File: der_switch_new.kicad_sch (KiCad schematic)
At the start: 1 part, among them U1 KSZ9477S

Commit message: add TQFP-128_14x14mm_P0.4mm_EP10x10mm_ThermalVias footprint
and assign it to the ksz chip

Signed-off-by: Oleksij Rempel <linux@rempel-privat.de>
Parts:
- U1: footprint Package_QFP:TQFP-128_14x14mm_P0.4mm -> footprints:TQFP-128_14x14mm_P0.4mm_EP10x10mm_ThermalVias
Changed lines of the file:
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@@
       (effects (font (size 1.27 1.27)) (justify left))
     )
-    (property "Footprint" "Package_QFP:TQFP-128_14x14mm_P0.4mm" (id 2) (at 233.426 144.272 0)
+    (property "Footprint" "footprints:TQFP-128_14x14mm_P0.4mm_EP10x10mm_ThermalVias" (id 2) (at 233.426 144.272 0)
       (effects (font (size 1.27 1.27)) hide)
     )
@@
     (property "Reference" "U1" (id 0) (at 62.23 21.59 0))
     (property "Value" "KSZ9477S" (id 1) (at 62.23 24.13 0))
-    (property "Footprint" "Package_QFP:TQFP-128_14x14mm_P0.4mm" (id 2) (at 46.736 62.992 0)
+    (property "Footprint" "footprints:TQFP-128_14x14mm_P0.4mm_EP10x10mm_ThermalVias" (id 2) (at 46.736 62.992 0)
       (effects (font (size 1.27 1.27)) hide)
     )
@@
       (effects (font (size 1.27 1.27)) (justify left))
     )
-    (property "Footprint" "Package_QFP:TQFP-128_14x14mm_P0.4mm" (id 2) (at 182.626 126.492 0)
+    (property "Footprint" "footprints:TQFP-128_14x14mm_P0.4mm_EP10x10mm_ThermalVias" (id 2) (at 182.626 126.492 0)
       (effects (font (size 1.27 1.27)) hide)
     )
@@
   (symbol_instances
     (path "/80ef473c-1a77-4105-9e67-974a5bdd257e"
-      (reference "U1") (unit 1) (value "KSZ9477S") (footprint "Package_QFP:TQFP-128_14x14mm_P0.4mm")
+      (reference "U1") (unit 1) (value "KSZ9477S") (footprint "footprints:TQFP-128_14x14mm_P0.4mm_EP10x10mm_ThermalVias")
     )
     (path "/21ac9210-ce64-4f1c-8b3c-e40224109109"
-      (reference "U1") (unit 7) (value "KSZ9477S") (footprint "Package_QFP:TQFP-128_14x14mm_P0.4mm")
+      (reference "U1") (unit 7) (value "KSZ9477S") (footprint "footprints:TQFP-128_14x14mm_P0.4mm_EP10x10mm_ThermalVias")
     )
     (path "/8afa4008-8209-42cc-9fef-0c59ffa66b4d"
-      (reference "U1") (unit 8) (value "KSZ9477S") (footprint "Package_QFP:TQFP-128_14x14mm_P0.4mm")
+      (reference "U1") (unit 8) (value "KSZ9477S") (footprint "footprints:TQFP-128_14x14mm_P0.4mm_EP10x10mm_ThermalVias")
     )
     (path "/71aecc81-5a5e-4293-ac09-31c20a082000/64182846-cada-49dd-8527-6959da40f69f"
@@
     )
     (path "/71aecc81-5a5e-4293-ac09-31c20a082000/9e4a7f6b-5383-44a7-b0de-9b68ac0e96b4"
-      (reference "U1") (unit 9) (value "KSZ9477S") (footprint "Package_QFP:TQFP-128_14x14mm_P0.4mm")
+      (reference "U1") (unit 9) (value "KSZ9477S") (footprint "footprints:TQFP-128_14x14mm_P0.4mm_EP10x10mm_ThermalVias")
     )
     (path "/33923bc8-5675-46d6-90be-4bb312e65519/a0f59906-4c59-4b83-9dc6-53f2550f4015"
@@
     )
     (path "/33923bc8-5675-46d6-90be-4bb312e65519/3e63a1df-1271-48f3-b68c-81f417692ad7"
-      (reference "U1") (unit 6) (value "KSZ9477S") (footprint "Package_QFP:TQFP-128_14x14mm_P0.4mm")
+      (reference "U1") (unit 6) (value "KSZ9477S") (footprint "footprints:TQFP-128_14x14mm_P0.4mm_EP10x10mm_ThermalVias")
     )
     (path "/33923bc8-5675-46d6-90be-4bb312e65519/5b33dfef-7c88-4a53-adf9-8d0c01072e7c/708f89c6-cb28-4190-913e-6f6103f78790"
@@
     )
     (path "/33923bc8-5675-46d6-90be-4bb312e65519/5b33dfef-7c88-4a53-adf9-8d0c01072e7c/ff5fbc13-5ce9-4122-a56a-496076beffc2"
-      (reference "U1") (unit 2) (value "KSZ9477S") (footprint "Package_QFP:TQFP-128_14x14mm_P0.4mm")
+      (reference "U1") (unit 2) (value "KSZ9477S") (footprint "footprints:TQFP-128_14x14mm_P0.4mm_EP10x10mm_ThermalVias")
     )
     (path "/33923bc8-5675-46d6-90be-4bb312e65519/5b33dfef-7c88-4a53-adf9-8d0c01072e7c/860177f5-e5f9-4667-bdf1-260227f40112"
-      (reference "U1") (unit 3) (value "KSZ9477S") (footprint "Package_QFP:TQFP-128_14x14mm_P0.4mm")
+      (reference "U1") (unit 3) (value "KSZ9477S") (footprint "footprints:TQFP-128_14x14mm_P0.4mm_EP10x10mm_ThermalVias")
     )
     (path "/33923bc8-5675-46d6-90be-4bb312e65519/c8a14ab9-546c-463a-ad16-fe3e65a560b9/eb7b83be-b0ce-45b6-906a-1b3b0cc9f6ff"
@@
     )
     (path "/33923bc8-5675-46d6-90be-4bb312e65519/c8a14ab9-546c-463a-ad16-fe3e65a560b9/639c0f21-cd49-4621-910a-9ec66a1169ab"
-      (reference "U1") (unit 4) (value "KSZ9477S") (footprint "Package_QFP:TQFP-128_14x14mm_P0.4mm")
+      (reference "U1") (unit 4) (value "KSZ9477S") (footprint "footprints:TQFP-128_14x14mm_P0.4mm_EP10x10mm_ThermalVias")
     )
     (path "/33923bc8-5675-46d6-90be-4bb312e65519/c8a14ab9-546c-463a-ad16-fe3e65a560b9/08269ac5-7f42-4ff7-a5e8-908b55ba521c"
-      (reference "U1") (unit 5) (value "KSZ9477S") (footprint "Package_QFP:TQFP-128_14x14mm_P0.4mm")
-    )
-  )
+      (reference "U1") (unit 5) (value "KSZ9477S") (footprint "footprints:TQFP-128_14x14mm_P0.4mm_EP10x10mm_ThermalVias")
+    )
+  )

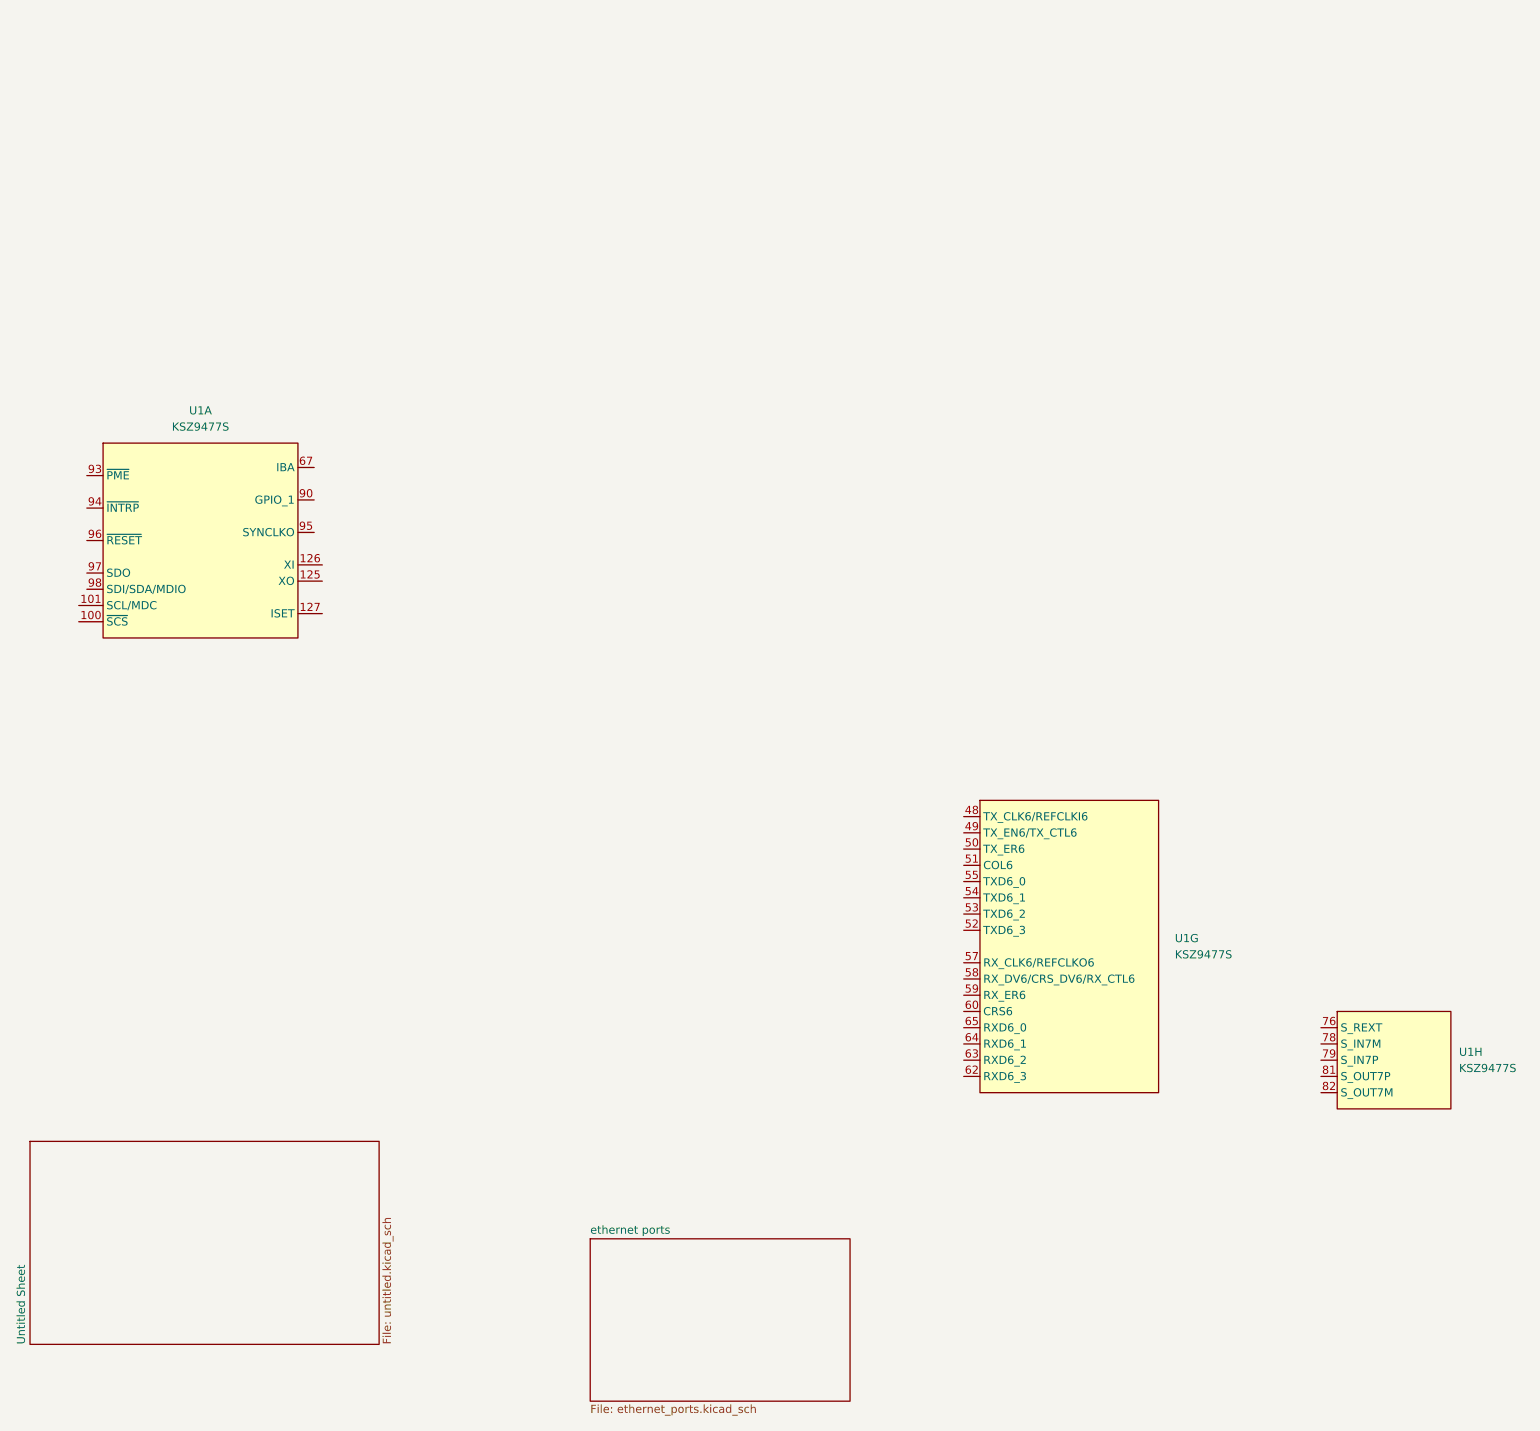
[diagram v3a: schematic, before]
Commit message: update pin naming. use _P/_N to allow optiomisation for differential signal
Signed-off-by: Oleksij Rempel <linux@rempel-privat.de>
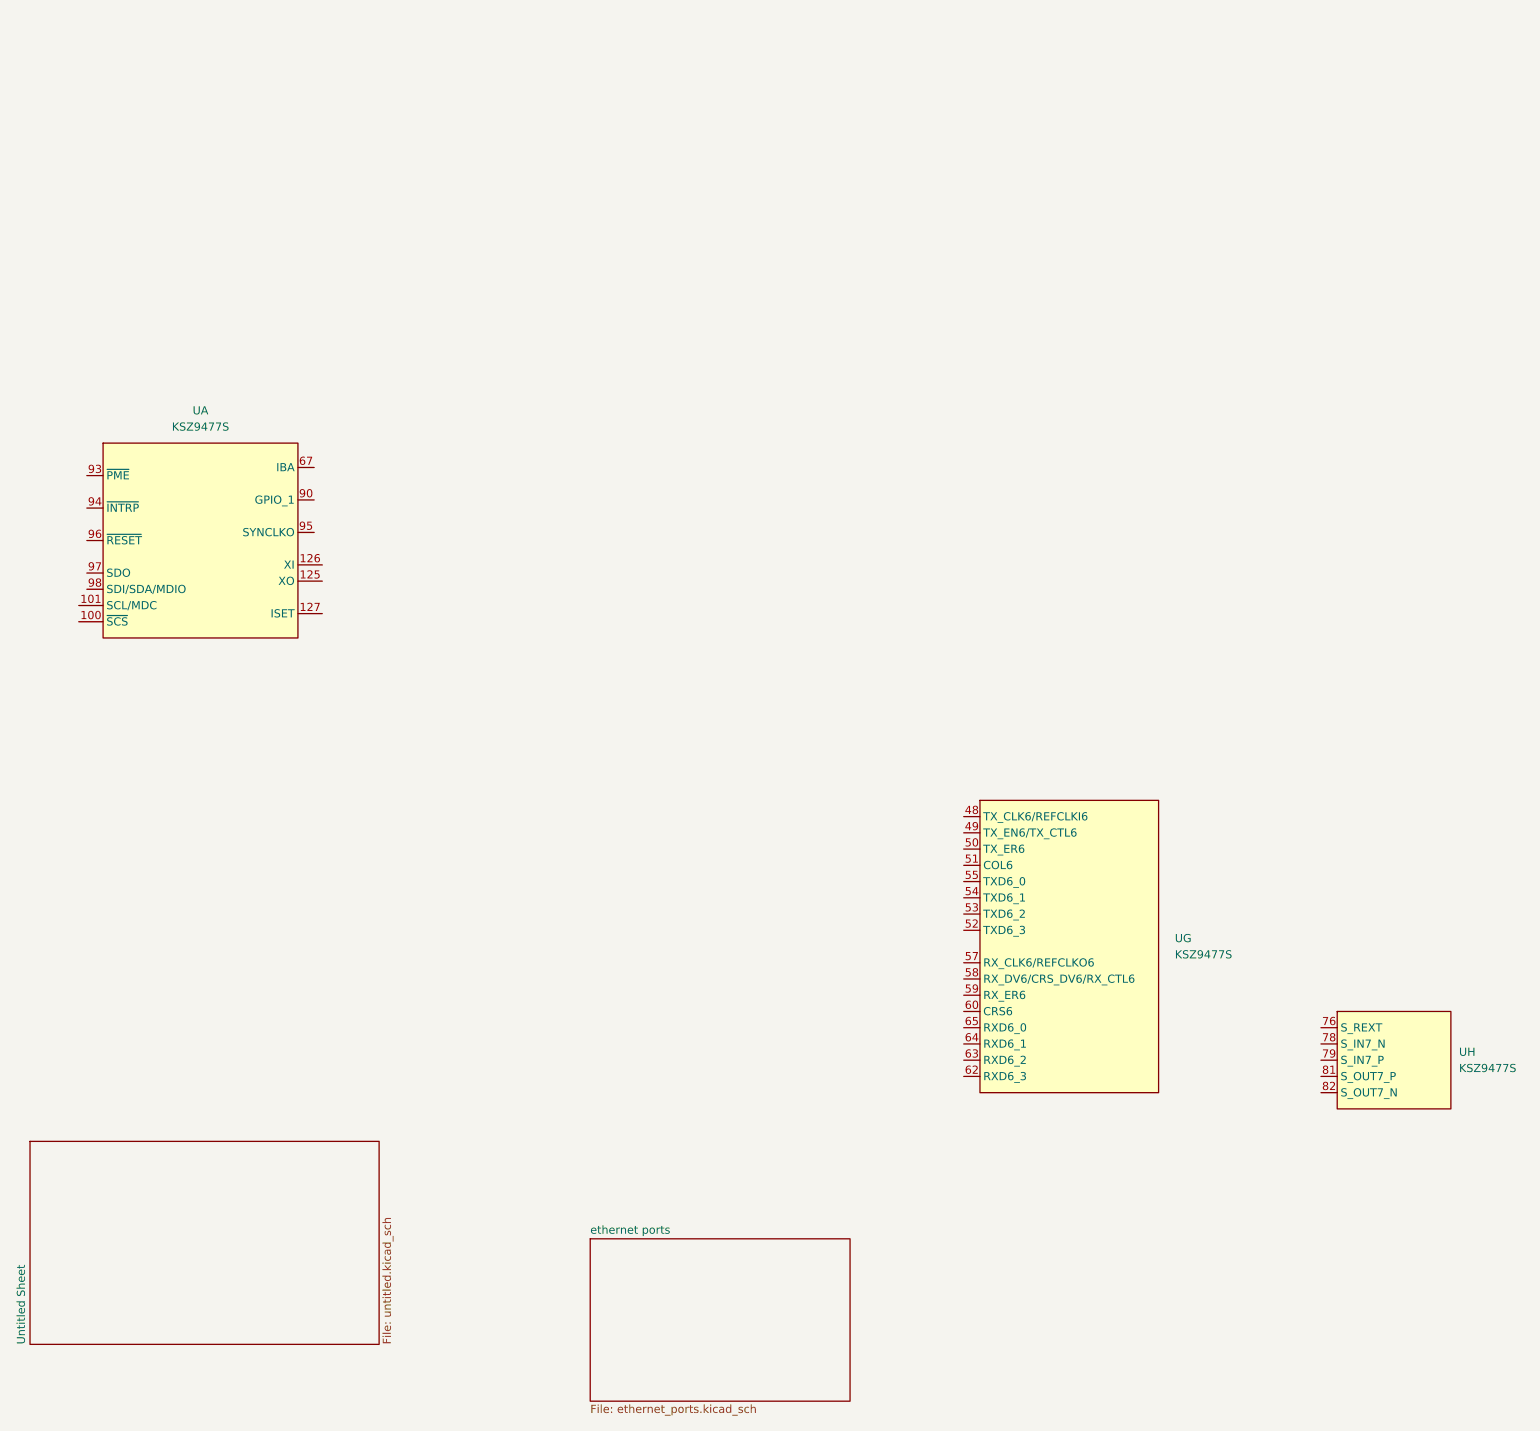
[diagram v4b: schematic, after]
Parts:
- U: renamed from U1; footprint footprints:TQFP-128_14x14mm_P0.4mm_EP10x10mm_ThermalVias -> Package_QFP:TQFP-128_14x14mm_P0.4mm
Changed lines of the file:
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@@
-(kicad_sch (version 20201015) (generator eeschema)
+(kicad_sch (version 20210126) (generator eeschema)
   (paper "A4")
-  (symbol (lib_id "local:KSZ9477S") (at 248.92 123.19 0) (unit 8)
+  (symbol (lib_name "local:KSZ9477S_2") (lib_id "local:KSZ9477S") (at 248.92 123.19 0) (unit 8)
     (in_bom yes) (on_board yes)
-    (property "Reference" "U1" (id 0) (at 259.08 121.92 0)
+    (property "Reference" "U" (id 0) (at 259.08 121.92 0)
       (effects (font (size 1.27 1.27)) (justify left))
     )
@@
       (effects (font (size 1.27 1.27)) (justify left))
     )
-    (property "Footprint" "footprints:TQFP-128_14x14mm_P0.4mm_EP10x10mm_ThermalVias" (id 2) (at 233.426 144.272 0)
+    (property "Footprint" "Package_QFP:TQFP-128_14x14mm_P0.4mm" (id 2) (at 233.426 144.272 0)
       (effects (font (size 1.27 1.27)) hide)
     )
@@
       (effects (font (size 1.27 1.27)) hide)
     )
-  )
-  (symbol (lib_id "local:KSZ9477S") (at 62.23 41.91 0) (unit 1)
+    (pin "76")
+    (pin "82")
+    (pin "81")
+    (pin "78")
+    (pin "79")
+  )
+  (symbol (lib_name "local:KSZ9477S_1") (lib_id "local:KSZ9477S") (at 62.23 41.91 0) (unit 1)
     (in_bom yes) (on_board yes)
-    (property "Reference" "U1" (id 0) (at 62.23 21.59 0))
+    (property "Reference" "U" (id 0) (at 62.23 21.59 0))
     (property "Value" "KSZ9477S" (id 1) (at 62.23 24.13 0))
-    (property "Footprint" "footprints:TQFP-128_14x14mm_P0.4mm_EP10x10mm_ThermalVias" (id 2) (at 46.736 62.992 0)
+    (property "Footprint" "Package_QFP:TQFP-128_14x14mm_P0.4mm" (id 2) (at 46.736 62.992 0)
       (effects (font (size 1.27 1.27)) hide)
     )
@@
       (effects (font (size 1.27 1.27)) hide)
     )
+    (pin "97")
+    (pin "98")
+    (pin "100")
+    (pin "101")
+    (pin "125")
+    (pin "126")
+    (pin "93")
+    (pin "94")
+    (pin "96")
+    (pin "95")
+    (pin "90")
+    (pin "127")
+    (pin "67")
+    (pin "73")
+    (pin "74")
+    (pin "108")
   )
   (symbol (lib_id "local:KSZ9477S") (at 198.12 105.41 0) (unit 7)
     (in_bom yes) (on_board yes)
-    (property "Reference" "U1" (id 0) (at 214.63 104.14 0)
+    (property "Reference" "U" (id 0) (at 214.63 104.14 0)
       (effects (font (size 1.27 1.27)) (justify left))
     )
@@
       (effects (font (size 1.27 1.27)) (justify left))
     )
-    (property "Footprint" "footprints:TQFP-128_14x14mm_P0.4mm_EP10x10mm_ThermalVias" (id 2) (at 182.626 126.492 0)
+    (property "Footprint" "Package_QFP:TQFP-128_14x14mm_P0.4mm" (id 2) (at 182.626 126.492 0)
       (effects (font (size 1.27 1.27)) hide)
     )
@@
       (effects (font (size 1.27 1.27)) hide)
     )
+    (pin "62")
+    (pin "63")
+    (pin "64")
+    (pin "65")
+    (pin "57")
+    (pin "58")
+    (pin "59")
+    (pin "52")
+    (pin "53")
+    (pin "54")
+    (pin "55")
+    (pin "48")
+    (pin "49")
+    (pin "50")
+    (pin "51")
+    (pin "60")
   )
   (sheet (at 35.56 135.89) (size 54.61 31.75)
@@
       (effects (font (size 1.27 1.27)) (justify left bottom))
     )
-    (property "Sheet file" "untitled.kicad_sch" (id 1) (at 90.6789 167.64 90)
+    (property "Dateiname Blatt" "untitled.kicad_sch" (id 1) (at 90.6789 167.64 90)
       (effects (font (size 1.27 1.27)) (justify left top))
     )
@@
       (effects (font (size 1.27 1.27)) (justify left bottom))
     )
-    (property "Sheet file" "ethernet_ports.kicad_sch" (id 1) (at 123.19 177.0389 0)
+    (property "Dateiname Blatt" "ethernet_ports.kicad_sch" (id 1) (at 123.19 177.0389 0)
       (effects (font (size 1.27 1.27)) (justify left top))
     )
@@
   (symbol_instances
     (path "/80ef473c-1a77-4105-9e67-974a5bdd257e"
-      (reference "U1") (unit 1) (value "KSZ9477S") (footprint "footprints:TQFP-128_14x14mm_P0.4mm_EP10x10mm_ThermalVias")
+      (reference "U") (unit 1) (value "KSZ9477S") (footprint "Package_QFP:TQFP-128_14x14mm_P0.4mm")
     )
     (path "/21ac9210-ce64-4f1c-8b3c-e40224109109"
-      (reference "U1") (unit 7) (value "KSZ9477S") (footprint "footprints:TQFP-128_14x14mm_P0.4mm_EP10x10mm_ThermalVias")
+      (reference "U") (unit 7) (value "KSZ9477S") (footprint "Package_QFP:TQFP-128_14x14mm_P0.4mm")
     )
     (path "/8afa4008-8209-42cc-9fef-0c59ffa66b4d"
-      (reference "U1") (unit 8) (value "KSZ9477S") (footprint "footprints:TQFP-128_14x14mm_P0.4mm_EP10x10mm_ThermalVias")
+      (reference "U") (unit 8) (value "KSZ9477S") (footprint "Package_QFP:TQFP-128_14x14mm_P0.4mm")
     )
     (path "/71aecc81-5a5e-4293-ac09-31c20a082000/64182846-cada-49dd-8527-6959da40f69f"
@@
     )
     (path "/71aecc81-5a5e-4293-ac09-31c20a082000/9e4a7f6b-5383-44a7-b0de-9b68ac0e96b4"
-      (reference "U1") (unit 9) (value "KSZ9477S") (footprint "footprints:TQFP-128_14x14mm_P0.4mm_EP10x10mm_ThermalVias")
+      (reference "U") (unit 9) (value "KSZ9477S") (footprint "Package_QFP:TQFP-128_14x14mm_P0.4mm")
     )
     (path "/33923bc8-5675-46d6-90be-4bb312e65519/a0f59906-4c59-4b83-9dc6-53f2550f4015"
@@
     )
     (path "/33923bc8-5675-46d6-90be-4bb312e65519/3e63a1df-1271-48f3-b68c-81f417692ad7"
-      (reference "U1") (unit 6) (value "KSZ9477S") (footprint "footprints:TQFP-128_14x14mm_P0.4mm_EP10x10mm_ThermalVias")
+      (reference "U") (unit 6) (value "KSZ9477S") (footprint "Package_QFP:TQFP-128_14x14mm_P0.4mm")
     )
     (path "/33923bc8-5675-46d6-90be-4bb312e65519/5b33dfef-7c88-4a53-adf9-8d0c01072e7c/708f89c6-cb28-4190-913e-6f6103f78790"
@@
     )
     (path "/33923bc8-5675-46d6-90be-4bb312e65519/5b33dfef-7c88-4a53-adf9-8d0c01072e7c/ff5fbc13-5ce9-4122-a56a-496076beffc2"
-      (reference "U1") (unit 2) (value "KSZ9477S") (footprint "footprints:TQFP-128_14x14mm_P0.4mm_EP10x10mm_ThermalVias")
+      (reference "U") (unit 2) (value "KSZ9477S") (footprint "Package_QFP:TQFP-128_14x14mm_P0.4mm")
     )
     (path "/33923bc8-5675-46d6-90be-4bb312e65519/5b33dfef-7c88-4a53-adf9-8d0c01072e7c/860177f5-e5f9-4667-bdf1-260227f40112"
-      (reference "U1") (unit 3) (value "KSZ9477S") (footprint "footprints:TQFP-128_14x14mm_P0.4mm_EP10x10mm_ThermalVias")
+      (reference "U") (unit 3) (value "KSZ9477S") (footprint "Package_QFP:TQFP-128_14x14mm_P0.4mm")
     )
     (path "/33923bc8-5675-46d6-90be-4bb312e65519/c8a14ab9-546c-463a-ad16-fe3e65a560b9/eb7b83be-b0ce-45b6-906a-1b3b0cc9f6ff"
@@
     )
     (path "/33923bc8-5675-46d6-90be-4bb312e65519/c8a14ab9-546c-463a-ad16-fe3e65a560b9/639c0f21-cd49-4621-910a-9ec66a1169ab"
-      (reference "U1") (unit 4) (value "KSZ9477S") (footprint "footprints:TQFP-128_14x14mm_P0.4mm_EP10x10mm_ThermalVias")
+      (reference "U") (unit 4) (value "KSZ9477S") (footprint "Package_QFP:TQFP-128_14x14mm_P0.4mm")
     )
     (path "/33923bc8-5675-46d6-90be-4bb312e65519/c8a14ab9-546c-463a-ad16-fe3e65a560b9/08269ac5-7f42-4ff7-a5e8-908b55ba521c"
-      (reference "U1") (unit 5) (value "KSZ9477S") (footprint "footprints:TQFP-128_14x14mm_P0.4mm_EP10x10mm_ThermalVias")
-    )
-  )
+      (reference "U") (unit 5) (value "KSZ9477S") (footprint "Package_QFP:TQFP-128_14x14mm_P0.4mm")
+    )
+  )
